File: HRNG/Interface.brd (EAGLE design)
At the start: 57.8 x 21 mm, 16 parts, among them IC1 LM358N, IC2 FT232RL, J1 PIC_ICSP_6_PINPOLAR_LOCK, J2 USB_MINI-B_SMT

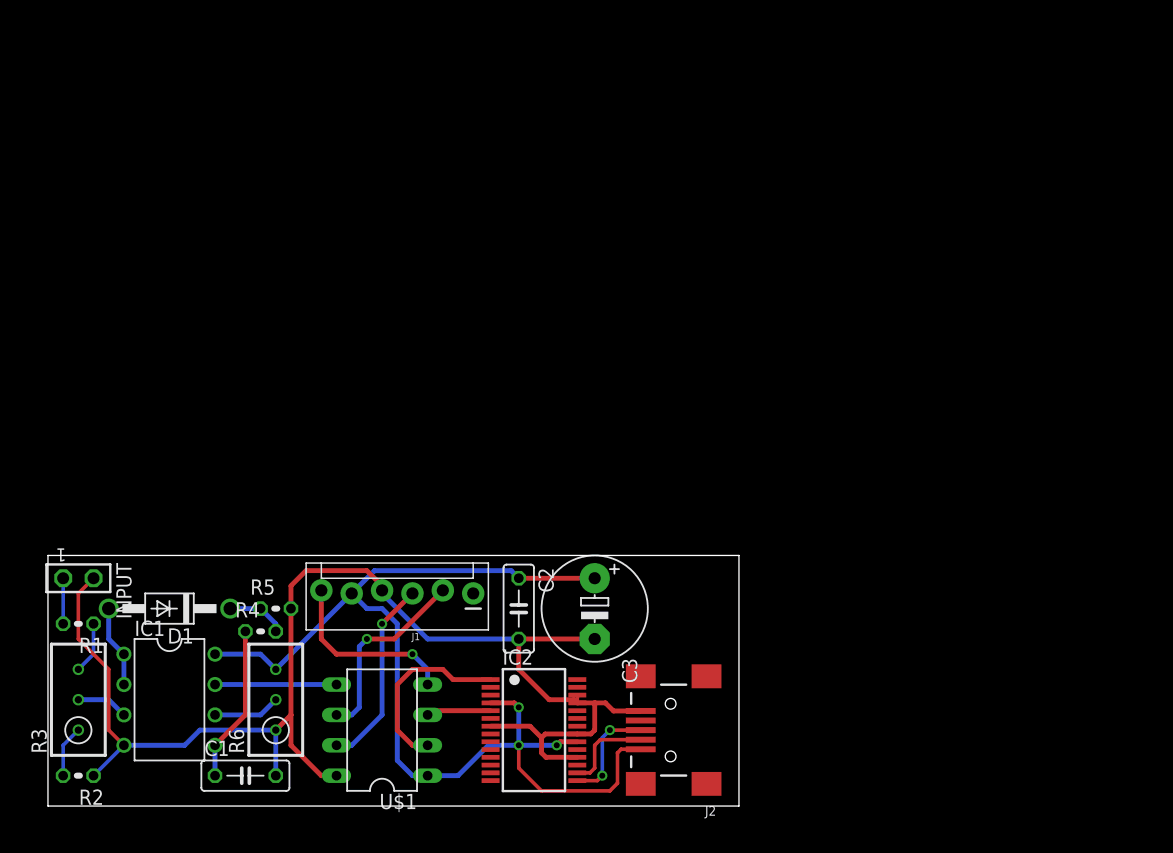
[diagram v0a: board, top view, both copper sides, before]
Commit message: Encrypter work
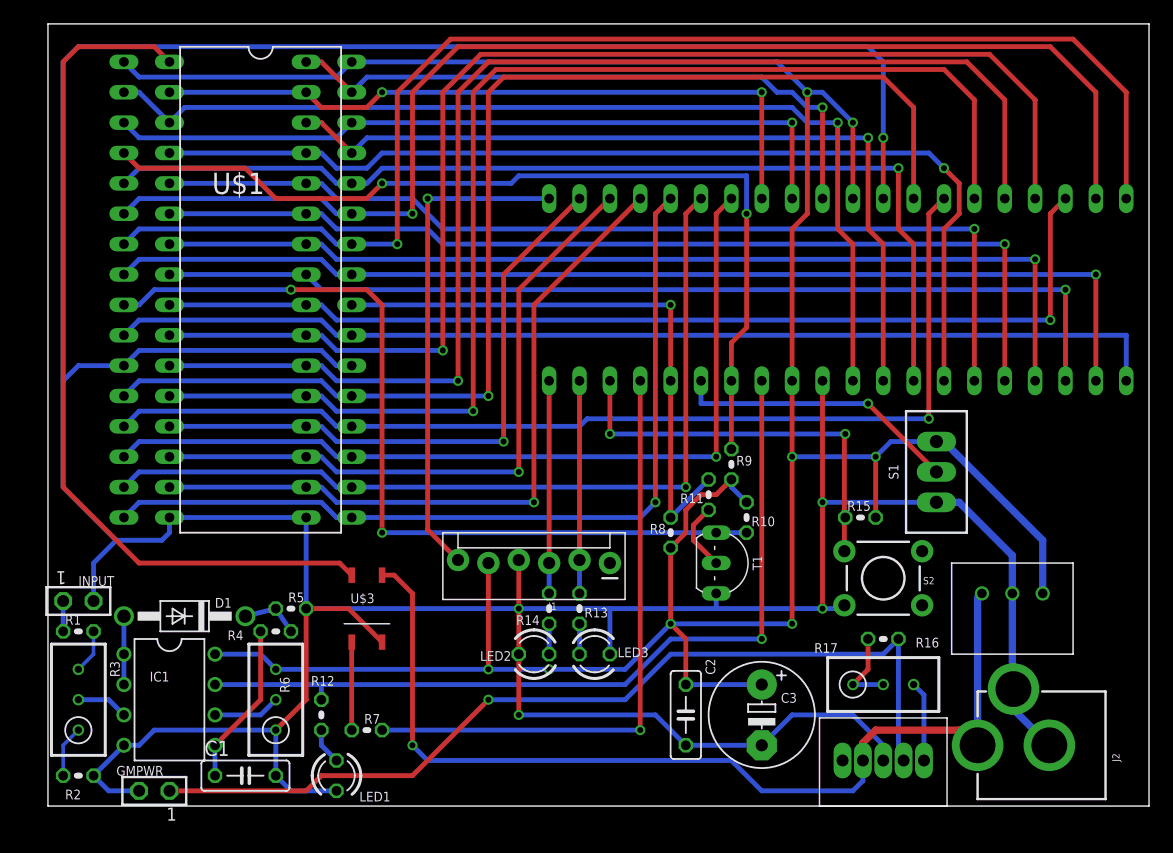
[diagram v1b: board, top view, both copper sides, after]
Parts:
- removed IC2: FT232RL, ftdichip:SSOP28
- added GMPWR: TSW-102-02-S-S, con-samtec:TSW-102-02-S-S
- added IC3: PIC16F1517/19P, microchip:DIL40
- added LED1, LED2, LED3: (no value), led:LED3MM
- added R10, R8, R9: 10k, resistor:0204V
- added R11, R12, R13, R14, R15, R16, R7: (no value), resistor:0204V
- added R17: 50k, resistor:RTRIM3296W
- added S1: TL36PO, switch:TL3XPO
- added S2: MOMENTARY-SWITCH-SPST-PTH-6.0MM, SparkFun-Switches:TACTILE_SWITCH_PTH_6.0MM
- added T1: (no value), transistor:TO92-CBE
- added U$2: AS6C4008, Football:DIL32
- added U$3: CPC1008N, JSB2:SOP04
- added U$4: OKR-T/1.5-W12-C, Football:SIP5
- added U$5: OKI-78SR-5/1.5-W36-C, JSB2:SIP_PS
- J2: value USB_MINI-B_SMT -> POWER_JACK; device SparkFun-Connectors:USB-MINIB -> SparkFun-Connectors:POWER_JACK_PTH
- U$1: value PIC16F18313 -> AT27C040; device PIC16:DIL08 -> Football:DIL32
- moved J2 39.4 mm to (91.4, 5.08), turned to 90 degrees
- moved U$1 38.2 mm to (17.8, 43.2), turned to 270 degrees
- moved C2 16.6 mm to (53.3, 7.62)
- moved C3 16.6 mm to (59.7, 7.62)
- moved J1 11.7 mm to (47.0, 20.3)
- moved INPUT 1.91 mm to (2.54, 17.1)
- moved D1 1.42 mm to (11.4, 15.9)
- moved R4 1.27 mm to (19.1, 14.6)
- moved R5 1.27 mm to (20.3, 16.5)
- moved R1 0.63 mm to (2.54, 14.6)
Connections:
- new net +12V: J2.PWR, U$3.4, U$4.P$2, U$5.P$1
- new net A0: IC3.15, U$1.12, U$2.12
- new net A1: IC3.16, U$1.11, U$2.11
- new net A10: IC3.21, U$1.23, U$2.23
- new net A11: IC3.22, U$1.25, U$2.25
- new net A12: IC3.27, U$1.4, U$2.4
- new net A13: IC3.28, U$1.28, U$2.28
- new net A14: IC3.29, U$1.29, U$2.3
- new net A15: IC3.30, U$1.3, U$2.31
- new net A16: IC3.8, U$1.2, U$2.2
- new net A17: IC3.9, U$1.30, U$2.30
- new net A18: IC3.10, U$1.31, U$2.1
- new net A2: IC3.17, U$1.10, U$2.10
- new net A3: IC3.18, U$1.9, U$2.9
- new net A4: IC3.23, U$1.8, U$2.8
- new net A5: IC3.24, U$1.7, U$2.7
- new net A6: IC3.25, U$1.6, U$2.6
- new net A7: IC3.26, U$1.5, U$2.5
- new net A8: IC3.19, U$1.27, U$2.27
- new net A9: IC3.20, U$1.26, U$2.26
- new net D0: IC3.2, U$1.13, U$2.13
- new net D1: IC3.3, U$1.14, U$2.14
- new net D2: IC3.4, U$1.15, U$2.15
- new net D3: IC3.5, U$1.17, U$2.17
- new net D4: IC3.6, U$1.18, U$2.18
- new net D5: IC3.7, U$1.19, U$2.19
- new net D6: IC3.14, U$1.20, U$2.20
- new net D7: IC3.13, U$1.21, U$2.21
- new net N$15: IC3.1, J1.6
- new net N$16: U$1.1, U$3.6
- new net N$19: R10.2, T1.C, U$2.24
- new net N$20: LED1.A, R12.2
- new net N$21: IC3.35, S1.2
- new net N$22: LED2.A, R14.2
- new net N$23: LED3.A, R13.2
- new net N$24: IC3.38, R15.2, S2.1
- new net N$25: GMPWR.1, R16.1, U$4.P$4
- new net N$26: R17.3, U$4.P$5
- new net N$27: R16.2, R17.1, R17.2
- net +5V: now also IC3.11, IC3.32, R10.1, R15.1, R8.1, R9.1, S1.3, U$1.32, U$2.32, U$5.P$3; no longer IC2.20, IC2.4, J2.VBUS, U$1.1
- net GND: now also GMPWR.2, IC3.12, IC3.31, J2.GNDBREAK, LED1.K, LED2.K, LED3.K, S1.1, S2.3, T1.E, U$1.16, U$1.22, U$2.16, U$2.22, U$3.3, U$4.P$3, U$5.P$2; no longer IC2.18, IC2.21, IC2.25, IC2.26, IC2.7, U$1.8
- net N$10: now also IC3.40, J1.3, R14.1; no longer J1.2, U$1.6
- net N$11: now also IC3.34, R9.2, U$2.29; no longer J1.6, U$1.4
- net N$12: now also R11.1, T1.B; no longer IC1.7, U$1.5
- net N$13: now also IC3.36, R11.2, R8.2, U$1.24; no longer IC2.15, J2.D+
- net N$14: now also IC1.7, IC3.33, R12.1; no longer IC2.16, J2.D-
- net N$17: now also R7.1, U$3.1; no longer IC2.1, U$1.2
- net N$18: now also IC3.37, R7.2; no longer IC2.5, U$1.3
- net N$9: now also IC3.39, J1.2, R13.1; no longer J1.3, U$1.7
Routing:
- net GND: track 116.2 -> 380.8 mm, vias 0 -> 5
- net +5V: track 90.5 -> 238.4 mm, vias 3 -> 8
- net A9: track 0.00 -> 110.1 mm, vias 0 -> 1
- net A2: track 0.00 -> 105.7 mm, vias 0 -> 1
- net A1: track 0.00 -> 105.1 mm, vias 0 -> 1
- net A0: track 0.00 -> 104.6 mm, vias 0 -> 1
- net A8: track 0.00 -> 104.5 mm, vias 0 -> 1
- net D7: track 0.00 -> 101.7 mm, vias 0 -> 1
- net A11: track 0.00 -> 91.2 mm, vias 0 -> 1
- net A10: track 0.00 -> 88.7 mm
- net D6: track 0.00 -> 87.6 mm, vias 0 -> 1
- net A12: track 0.00 -> 85.2 mm, vias 0 -> 1
- net A3: track 0.00 -> 84.9 mm, vias 0 -> 1
- net A13: track 0.00 -> 84.7 mm, vias 0 -> 1
- net A15: track 0.00 -> 83.9 mm, vias 0 -> 1
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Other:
- board size 57.8 x 21 mm -> 92.1 x 65.4 mm

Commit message: Board updates
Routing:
- net GND: track 380.8 -> 294.4 mm
- net A1: track 105.1 -> 94.0 mm
- net A2: track 105.7 -> 94.5 mm
- net A8: track 104.5 -> 94.1 mm
- net A0: track 104.6 -> 94.2 mm
- net A9: track 110.1 -> 99.7 mm
- net D7: track 101.7 -> 92.8 mm
- net N$16: track 72.7 -> 68.7 mm
- net N$15: track 41.4 -> 40.0 mm
- net +12V: track 82.1 -> 83.1 mm
